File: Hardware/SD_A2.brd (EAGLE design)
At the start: 100.2 x 77.7 mm, 30 parts, among them IC1 74HCT245N, IC2 LM317, IC3 2716 / 2732, IC4 XC9572XL

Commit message: Small changes on board
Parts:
- C2: device rcl:E2,5-5 -> rcl:153CLV-0405
- moved C2 0.76 mm to (74.7, 21.1), turned to 0 degrees
- moved R4 0.50 mm to (57.1, 67.5)
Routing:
- net GND: track 50.0 -> 51.2 mm, vias 8 -> 9
- net N$29: track 2.68 -> 3.18 mm
- net !LED: track 32.4 -> 31.9 mm
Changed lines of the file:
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@@
 <?xml version="1.0" encoding="utf-8"?>
 <!DOCTYPE eagle SYSTEM "eagle.dtd">
-<eagle version="7.7.0">
+<eagle version="8.2.2">
 <drawing>
 <settings>
@@
 <attribute name="VALUE" x="86.31" y="25.007" size="1.778" layer="27" ratio="10" rot="R270"/>
 </element>
-<element name="C2" library="rcl" package="E2,5-5" value="1u" x="75.42731875" y="21.02" rot="R180"/>
+<element name="C2" library="rcl" library_urn="urn:adsk.eagle:library:334" package="153CLV-0405" value="1u" x="74.67268125" y="21.08"/>
 <element name="R1" library="rcl" package="R0603" value="200" x="79.99" y="27.74" smashed="yes">
 <attribute name="NAME" x="79.105" y="29.125" size="1.27" layer="25"/>
@@
 <attribute name="VALUE" x="88.645" y="37.145" size="1.27" layer="27" rot="R270"/>
 </element>
-<element name="R4" library="rcl" package="R0603" value="470" x="57.08" y="68.01" smashed="yes" rot="R270">
-<attribute name="NAME" x="58.465" y="69.145" size="1.27" layer="25" rot="R270"/>
-<attribute name="VALUE" x="55.175" y="68.645" size="1.27" layer="27" rot="R270"/>
+<element name="R4" library="rcl" package="R0603" value="470" x="57.08" y="67.51" smashed="yes" rot="R270">
+<attribute name="NAME" x="58.465" y="68.645" size="1.27" layer="25" rot="R270"/>
+<attribute name="VALUE" x="55.175" y="68.145" size="1.27" layer="27" rot="R270"/>
 </element>
 <element name="LED1" library="led" package="LED2X5" value="" x="57.11" y="72.8" rot="R270"/>
@@
 <contactref element="U$2" pad="SC"/>
 <contactref element="C1" pad="2"/>
-<wire x1="75.14" y1="27.77" x2="75.14" y2="24.64" width="0.4" layer="1"/>
-<wire x1="75.14" y1="24.64" x2="74.25" y2="23.75" width="0.4" layer="1"/>
-<wire x1="74.25" y1="23.75" x2="74.25" y2="21.11268125" width="0.4" layer="1"/>
-<wire x1="74.25" y1="21.11268125" x2="74.15731875" y2="21.02" width="0.4" layer="1"/>
-<wire x1="74.15731875" y1="21.02" x2="74.15731875" y2="20.59268125" width="0.4" layer="1"/>
-<wire x1="74.15731875" y1="20.59268125" x2="76.25" y2="18.5" width="0.4" layer="1"/>
-<wire x1="76.25" y1="18.5" x2="76.25" y2="16.625" width="0.4" layer="1"/>
 <wire x1="76.25" y1="16.625" x2="76.125" y2="16.5" width="0.4" layer="1"/>
 <via x="35.75" y="67.75" extent="1-16" drill="0.35"/>
@@
 <wire x1="88.265" y1="4.445" x2="88.265" y2="8.985" width="1" layer="16"/>
 <wire x1="88.265" y1="8.985" x2="88.25" y2="9" width="0.4" layer="16"/>
+<wire x1="76.125" y1="16.5" x2="76.125" y2="17.82768125" width="0.4" layer="1"/>
+<wire x1="72.87268125" y1="21.08" x2="76.125" y2="17.82768125" width="0.4" layer="1"/>
+<wire x1="75.14" y1="27.77" x2="75.14" y2="24.34" width="0.4" layer="1"/>
+<wire x1="75.14" y1="24.34" x2="75.1" y2="24.3" width="0.4" layer="1"/>
+<via x="75.1" y="24.3" extent="1-16" drill="0.35"/>
+<wire x1="75.1" y1="24.3" x2="75.1" y2="23.30731875" width="0.4" layer="1"/>
+<wire x1="75.1" y1="23.30731875" x2="72.87268125" y2="21.08" width="0.4" layer="1"/>
 </signal>
 <signal name="+5V">
@@
 <wire x1="88.265" y1="4.445" x2="88.265" y2="9.485" width="0.4" layer="1"/>
 <wire x1="88.265" y1="9.485" x2="86.25" y2="11.5" width="0.4" layer="1"/>
-<wire x1="80" y1="11.5" x2="86.25" y2="11.5" width="0.4" layer="1"/>
-<wire x1="79.93" y1="11.57" x2="79.96" y2="11.54" width="0.4" layer="1"/>
 <contactref element="SV1" pad="1"/>
 <contactref element="R10" pad="2"/>
@@
 <via x="56.75" y="14" extent="1-16" drill="0.35"/>
 <wire x1="56.75" y1="14" x2="56.75" y2="12.25" width="0.4" layer="1"/>
-<wire x1="56.75" y1="12.25" x2="57.5" y2="11.5" width="0.4" layer="1"/>
-<wire x1="57.5" y1="11.5" x2="80" y2="11.5" width="0.4" layer="1"/>
+<wire x1="57.5" y1="11.5" x2="56.75" y2="12.25" width="0.4" layer="1"/>
 <wire x1="49.29341875" y1="29.82" x2="46.29" y2="29.82" width="0.4" layer="16"/>
 <wire x1="49.29341875" y1="29.82" x2="56.68" y2="29.82" width="0.4" layer="16"/>
@@
 <wire x1="56.75" y1="29.75" x2="56.75" y2="14" width="0.4" layer="1"/>
 <contactref element="C1" pad="1"/>
-<wire x1="79.96" y1="14.247759375" x2="79.96" y2="16.52978125" width="0.4" layer="1"/>
-<wire x1="79.96" y1="14.247759375" x2="79.96" y2="13.969946875" width="0.4" layer="1"/>
-<wire x1="79.96" y1="16.52978125" x2="79.96" y2="18.53" width="0.4" layer="1"/>
-<wire x1="79.96" y1="13.969946875" x2="79.96" y2="11.54" width="0.4" layer="1"/>
-<wire x1="79.96" y1="11.54" x2="80" y2="11.5" width="0.4" layer="1"/>
-<wire x1="79.990053125" y1="14" x2="79.96" y2="13.969946875" width="0.4" layer="1"/>
+<wire x1="79.96" y1="18.53" x2="79.96" y2="16.52978125" width="0.4" layer="1"/>
 <wire x1="77.875" y1="16.5" x2="79.93021875" y2="16.5" width="0.4" layer="1"/>
 <wire x1="79.93021875" y1="16.5" x2="79.96" y2="16.52978125" width="0.4" layer="1"/>
-<wire x1="77.85" y1="14.25" x2="79.957759375" y2="14.25" width="0.4" layer="1"/>
-<wire x1="79.957759375" y1="14.25" x2="79.96" y2="14.247759375" width="0.4" layer="1"/>
 <wire x1="54" y1="15.375" x2="54" y2="14.182375" width="0.4" layer="16"/>
 <wire x1="54" y1="14.182375" x2="53.857625" y2="14.04" width="0.4" layer="16"/>
 <wire x1="49.25" y1="31.125" x2="49.25" y2="29.86341875" width="0.4" layer="16"/>
 <wire x1="49.25" y1="29.86341875" x2="49.29341875" y2="29.82" width="0.4" layer="16"/>
+<wire x1="79.955103125" y1="11.5" x2="86.25" y2="11.5" width="0.4" layer="1"/>
+<wire x1="79.955103125" y1="11.5" x2="57.5" y2="11.5" width="0.4" layer="1"/>
+<wire x1="79.96" y1="14.228103125" x2="79.96" y2="16.52978125" width="0.4" layer="1"/>
+<wire x1="79.96" y1="14.228103125" x2="79.96" y2="11.504896875" width="0.4" layer="1"/>
+<wire x1="79.96" y1="11.504896875" x2="79.955103125" y2="11.5" width="0.4" layer="1"/>
+<wire x1="77.85" y1="14.25" x2="79.938103125" y2="14.25" width="0.4" layer="1"/>
+<wire x1="79.938103125" y1="14.25" x2="79.96" y2="14.228103125" width="0.4" layer="1"/>
 </signal>
 <signal name="+3V3">
@@
 <wire x1="35.64" y1="60.5" x2="33" y2="57.86" width="0.4" layer="1"/>
 <wire x1="43.06" y1="60.5" x2="43.16" y2="60.4" width="0.4" layer="1"/>
-<wire x1="76.74731875" y1="21.07" x2="79.96" y2="21.07" width="0.4" layer="1"/>
-<wire x1="76.74731875" y1="21.07" x2="76.69731875" y2="21.02" width="0.4" layer="1"/>
-<wire x1="81.82" y1="21.07" x2="79.96" y2="21.07" width="0.4" layer="1"/>
+<wire x1="79.96" y1="21.07" x2="81.82" y2="21.07" width="0.4" layer="1"/>
 <wire x1="43.16" y1="70.56" x2="42.44" y2="70.56" width="0.4" layer="1"/>
 <wire x1="42.44" y1="70.56" x2="41.25" y2="71.75" width="0.4" layer="1"/>
@@
 <wire x1="40.7380625" y1="64.125" x2="39.93153125" y2="63.31846875" width="0.4" layer="16"/>
 <wire x1="83.2" y1="27.781146875" x2="83.2" y2="35.69103125" width="0.4" layer="1"/>
-<wire x1="83.2" y1="35.75" x2="83.2" y2="40.425" width="0.4" layer="1"/>
+<wire x1="83.2" y1="35.69103125" x2="83.2" y2="40.425" width="0.4" layer="1"/>
 <wire x1="83.2" y1="27.781146875" x2="83.2" y2="22.45" width="0.4" layer="1"/>
 <wire x1="83.2" y1="22.45" x2="81.82" y2="21.07" width="0.4" layer="1"/>
@@
 <wire x1="83.24103125" y1="35.65" x2="78.25" y2="35.65" width="0.4" layer="1"/>
 <wire x1="83.24103125" y1="35.65" x2="90.56" y2="35.65" width="0.4" layer="1"/>
-<wire x1="83.2" y1="35.75" x2="83.2" y2="35.69103125" width="0.4" layer="1"/>
 <wire x1="83.2" y1="35.69103125" x2="83.24103125" y2="35.65" width="0.4" layer="1"/>
+<wire x1="76.47268125" y1="21.08" x2="79.95" y2="21.08" width="0.4" layer="1"/>
+<wire x1="79.95" y1="21.08" x2="79.96" y2="21.07" width="0.4" layer="1"/>
 </signal>
 <signal name="N$1">
@@
 <contactref element="IC4" pad="29"/>
 <contactref element="R4" pad="2"/>
-<wire x1="57.08" y1="67.16" x2="57.08" y2="51.08" width="0.4" layer="1"/>
+<wire x1="57.08" y1="66.66" x2="57.08" y2="51.08" width="0.4" layer="1"/>
 <wire x1="57.08" y1="51.08" x2="57" y2="51" width="0.4" layer="1"/>
 <via x="57" y="51" extent="1-16" drill="0.35"/>
@@
 <contactref element="LED1" pad="K"/>
 <contactref element="R4" pad="1"/>
-<wire x1="57.11" y1="71.53" x2="57.11" y2="68.89" width="0.4" layer="1"/>
-<wire x1="57.11" y1="68.89" x2="57.08" y2="68.86" width="0.4" layer="1"/>
+<wire x1="57.11" y1="71.53" x2="57.11" y2="68.39" width="0.4" layer="1"/>
+<wire x1="57.11" y1="68.39" x2="57.08" y2="68.36" width="0.4" layer="1"/>
 </signal>
 <signal name="!G">
@@
 <contactref element="R10" pad="1"/>
 <wire x1="39" y1="74.25" x2="48.25" y2="74.25" width="0.4" layer="1"/>
-<wire x1="48.25" y1="74.25" x2="49.5" y2="73" width="0.4" layer="1"/>
+<wire x1="48.25" y1="74.25" x2="49.7" y2="72.8" width="0.4" layer="1"/>
 <wire x1="59.5" y1="12.5" x2="58.65" y2="13.35" width="0.4" layer="1"/>
 <wire x1="76.138959375" y1="12.5" x2="78" y2="12.5" width="0.4" layer="1"/>
@@
 <wire x1="78" y1="12.5" x2="78" y2="4.55" width="0.4" layer="16"/>
 <wire x1="78" y1="4.55" x2="78.105" y2="4.445" width="0.4" layer="16"/>
-<wire x1="57.75" y1="73" x2="49.5" y2="73" width="0.4" layer="1"/>
+<wire x1="57.75" y1="72.8" x2="49.7" y2="72.8" width="0.4" layer="1"/>
 <contactref element="IC4" pad="44"/>
 <wire x1="38.08" y1="73.1" x2="38.08" y2="73.33" width="0.4" layer="1"/>
 <wire x1="38.08" y1="73.33" x2="39" y2="74.25" width="0.4" layer="1"/>
-<wire x1="58.65" y1="72.1" x2="57.75" y2="73" width="0.4" layer="1"/>
-<wire x1="58.65" y1="13.35" x2="58.65" y2="72.1" width="0.4" layer="1"/>
+<wire x1="58.65" y1="71.9" x2="57.75" y2="72.8" width="0.4" layer="1"/>
+<wire x1="58.65" y1="13.35" x2="58.65" y2="71.9" width="0.4" layer="1"/>
 <wire x1="76.15" y1="14.25" x2="76.15" y2="12.511040625" width="0.4" layer="1"/>
 <wire x1="76.15" y1="12.511040625" x2="76.138959375" y2="12.5" width="0.4" layer="1"/>
@@
 which will not be processed correctly with this version.
 </note>
+<note version="8.2" severity="warning">
+Since Version 8.2, Eagle supports online libraries. The ids
+of those online libraries will not be understood (or retained)
+with this version.
+</note>
 </compatibility>

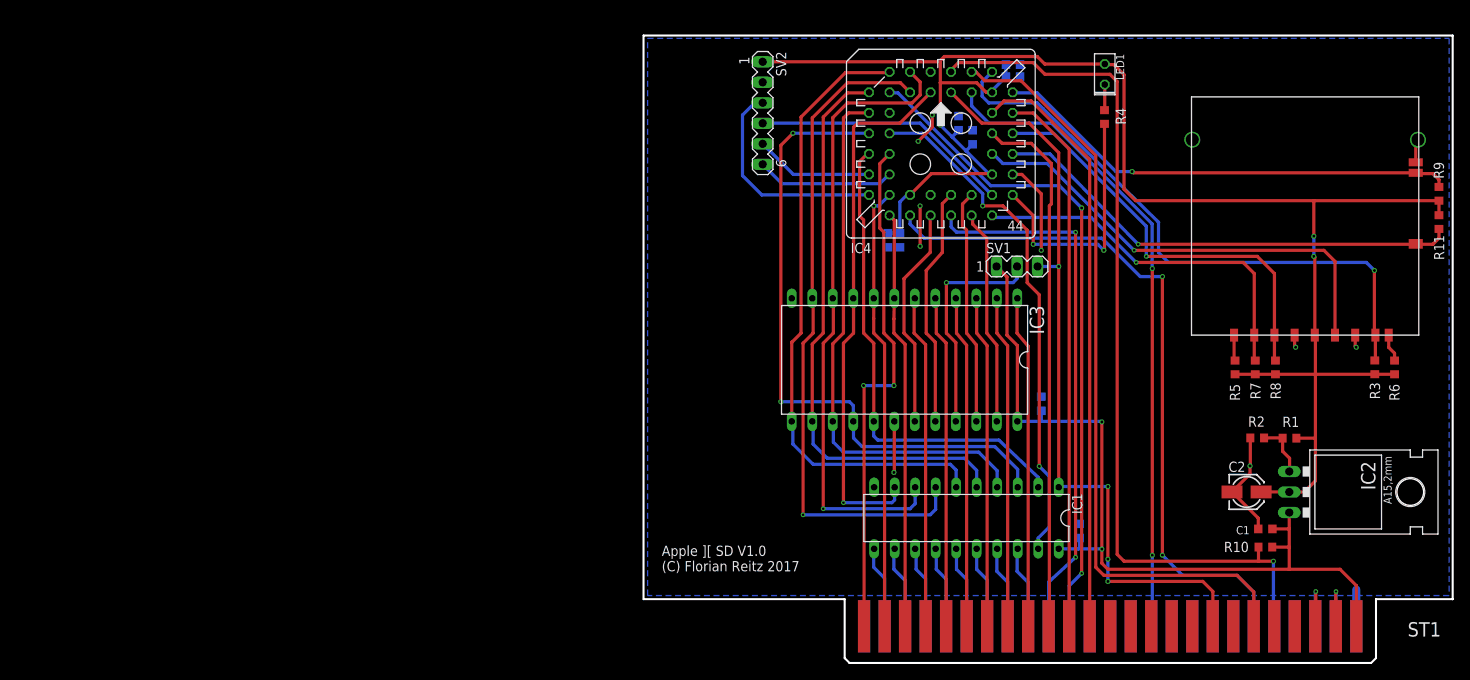
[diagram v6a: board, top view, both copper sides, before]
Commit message: IRQ Pin removed, A11 added
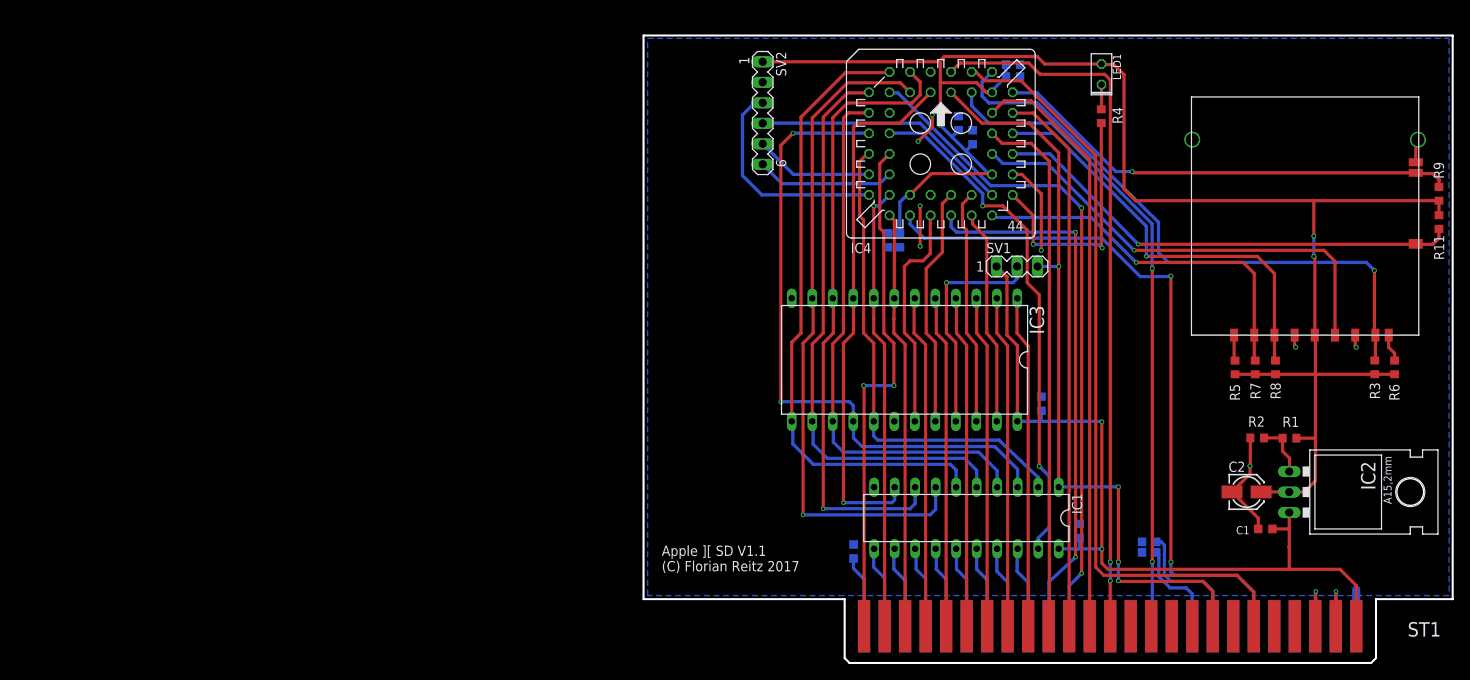
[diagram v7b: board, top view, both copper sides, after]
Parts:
- removed R10: 10k, rcl:R0603
- added C11, C12, C13: 100n, rcl:C0603K
- moved R4 0.41 mm to (56.7, 67.6)
- moved LED1 0.40 mm to (56.7, 72.8)
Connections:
- removed net !IRQ: IC4.44, R10.1, ST1.30
- new net +12V: C11.1, ST1.50
- new net -12V: C12.1, ST1.33
- new net -5V: C13.1, ST1.34
- new net ADD11: IC4.44, ST1.13
- net +5V: no longer R10.2
- net GND: now also C11.2, C12.2, C13.2
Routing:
- net !IRQ: track 110.3 -> 0.00 mm, vias 1 -> 0
- net ADD11: track 0.00 -> 88.7 mm, vias 0 -> 2
- net -12V: track 0.00 -> 16.1 mm
- net -5V: track 0.00 -> 12.2 mm
- net +12V: track 0.00 -> 8.92 mm
- net GND: track 51.2 -> 44.8 mm, vias 9 -> 8
- net +5V: track 105.3 -> 103.2 mm
- net !RESET: track 87.0 -> 88.2 mm
- net B10: track 27.4 -> 28.3 mm
- net !LED: track 31.9 -> 31.4 mm
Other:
- board text added: "Apple ][ SD V1.1 (C) Florian Reitz 2017"
- board text removed: "Apple ][ SD V1.0 (C) Florian Reitz 2017"

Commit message: Schematic updated
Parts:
- IC1: value 74HCT245N -> 74LS245N
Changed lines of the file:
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@@
 <attribute name="VALUE" x="34.27" y="76.148" size="1.27" layer="27" ratio="10"/>
 </element>
-<element name="IC1" library="74xx-eu" package="DIL20" value="74HCT245N" x="39.98" y="17.85" rot="R180"/>
+<element name="IC1" library="74xx-eu" library_urn="urn:adsk.eagle:library:85" package="DIL20" value="74LS245N" x="39.98" y="17.85" rot="R180"/>
 <element name="IC2" library="v-reg" package="317TL" value="LM317" x="83.77" y="21.07" smashed="yes" rot="R270">
 <attribute name="NAME" x="88.85" y="24.88" size="1.778" layer="25" ratio="10" rot="R270"/>
